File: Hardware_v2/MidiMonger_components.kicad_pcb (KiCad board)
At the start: 2 copper layers, 40 x 100 mm, 58 parts, among them J1 Conn_01x09_Male, J2 Conn_01x08_Male, J3 Conn_01x08_Male, J4 Conn_01x08_Male, J5 SWD_Header, J6 Eurorack_10_pin_power, U1 STM32F446RETx, U2 TL074, U3 74HCT244, U4 MAX5134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

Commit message: Updates to PCB layout
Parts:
- C16: footprint Capacitors_SMD:CP_Elec_5x5.3 -> Capacitor_SMD:CP_Elec_4x5.8
- C17: value 22uF -> 10uF; footprint Capacitors_SMD:CP_Elec_5x5.3 -> Capacitor_SMD:C_0805_2012Metric
- J2: value Conn_01x08_Male -> Conn_01x09_Male; footprint Connector_PinHeader_2.54mm:PinHeader_1x08_P2.54mm_Vertical -> Connector_PinHeader_2.54mm:PinHeader_1x09_P2.54mm_Vertical
- moved C17 68.0 mm to (114.1, 123.0), turned to 180 degrees
- moved R9 56.5 mm to (133.6, 75.9)
- moved R11 54.6 mm to (133.6, 78.4)
- moved R12 48.1 mm to (108.0, 75.7), turned to 0 degrees
- moved R17 44.8 mm to (108.8, 84.6), turned to 0 degrees
- moved R15 44.7 mm to (108.8, 82.9), turned to 0 degrees
- moved R14 44.1 mm to (133.6, 81.1), turned to 180 degrees
- moved R20 43.1 mm to (105.4, 112.5), turned to 0 degrees
- moved J5 38.4 mm to (138.0, 97.9), turned to -90 degrees
- moved R19 38.4 mm to (105.4, 110.9), turned to 0 degrees
- moved U5 37.7 mm to (120.0, 139.0), turned to 0 degrees
- moved R22 35.7 mm to (105.4, 115.7), turned to 0 degrees
- moved R21 33.3 mm to (105.4, 114.1), turned to 0 degrees
- moved R18 31.5 mm to (126.1, 130.5)
- moved R10 29.6 mm to (108.0, 72.3), turned to 0 degrees
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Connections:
- C12 pad 1: VCC -> +12V
- C13 pad 1: VCC -> +12V
- C16 pad 1: VCC -> +12V
- C17 pad 1: GND -> -12V
- C17 pad 2: VEE -> GND
- D2 pad 1: VCC -> +12V
- D2 pad 2: +12V -> /+12V_IN
- D3 pad 1: -12V -> /-12V_IN
- D3 pad 2: VEE -> -12V
- J1 pad 1: /CV1_OUT -> /GATE1_OUT
- J1 pad 2: /CV2_OUT -> /GATE2_LED_OUT
- J1 pad 3: GND -> /GATE3_OUT
- J1 pad 4: /CV3_OUT -> /GATE4_LED_OUT
- J1 pad 5: /CV4_OUT -> GND
- J1 pad 6: /CV1_LED_OUT -> /GATE5_OUT
- J1 pad 7: /CV2_LED_OUT -> /GATE6_LED_OUT
- J1 pad 8: /CV3_LED_OUT -> /GATE7_OUT
- J1 pad 9: /CV4_LED_OUT -> /GATE8_LED_OUT
- J2 pad 2: /GATE1_OUT -> /GATE2_OUT
- J2 pad 3: /GATE2_LED_OUT -> /GATE3_LED_OUT
- J2 pad 4: /GATE2_OUT -> /GATE4_OUT
- J2 pad 5: /GATE3_OUT -> GND
- J2 pad 6: /GATE3_LED_OUT -> /GATE5_LED_OUT
- J2 pad 7: /GATE4_OUT -> /GATE6_OUT
- J2 pad 8: /GATE4_LED_OUT -> /GATE8_OUT
- J3 pad 2: /GATE5_LED_OUT -> /CV1_LED_OUT
- J3 pad 3: GND -> /CV2_LED_OUT
- J3 pad 4: /GATE5_OUT -> /CV3_LED_OUT
- J3 pad 5: /GATE7_OUT -> /CV4_LED_OUT
- J3 pad 6: /USB_DP -> /MIDI_VREF
- J3 pad 7: /USB_DM -> /MIDI_DATA
- J3 pad 8: /USB_VBUS -> unconnected-(J3-Pin_8-Pad8)
- J4 pad 1: /GATE7_LED_OUT -> /USB_VBUS
- J4 pad 2: /GATE6_LED_OUT -> /USB_DM
- J4 pad 3: /GATE8_LED_OUT -> /USB_DP
- J4 pad 4: /GATE6_OUT -> GND
- J4 pad 5: /GATE8_OUT -> /CV3_OUT
- J4 pad 6: GND -> /CV2_OUT
- J4 pad 7: /MIDI_DATA -> /CV1_OUT
- J4 pad 8: /MIDI_VREF -> /CV4_OUT
- J6 pad 1: -12V -> /-12V_IN
- J6 pad 10: +12V -> /+12V_IN
- J6 pad 2: -12V -> /-12V_IN
- J6 pad 9: +12V -> /+12V_IN
- U1 pad 17: /GATE2 -> /GATE8
- U1 pad 21: /GATE3 -> /GATE6
- U1 pad 23: /GATE1 -> /GATE4
- U1 pad 24: unconnected-(U1-PC4-Pad24) -> /GATE2
- U1 pad 25: /GATE4 -> unconnected-(U1-PC5-Pad25)
- U1 pad 26: unconnected-(U1-PB0-Pad26) -> /GATE1
- U1 pad 28: /GATE6 -> /GATE3
- U1 pad 33: unconnected-(U1-PB12-Pad33) -> /GATE5
- U1 pad 35: unconnected-(U1-PB14-Pad35) -> /GATE7
- U1 pad 38: /GATE8 -> unconnected-(U1-PC7-Pad38)
- U1 pad 40: /GATE7 -> unconnected-(U1-PC9-Pad40)
- U1 pad 9: /GATE5 -> unconnected-(U1-PC1-Pad9)
- U2 pad 11: VEE -> -12V
- U2 pad 4: VCC -> +12V
- U6 pad 3: VCC -> +12V
- U7 pad 3: VCC -> +12V
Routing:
- net /CV4_OUT: track 2.87 -> 61.3 mm
- net /NRST: track 0.00 -> 48.4 mm
- net /USB_DP: track 0.00 -> 43.1 mm
- net /USB_DM: track 0.00 -> 41.7 mm
- net /USB_VBUS: track 0.00 -> 40.7 mm
- net /CV1_OUT: track 2.95 -> 35.5 mm
- net /CV3_OUT: track 2.87 -> 33.4 mm
- net /GATE5: track 0.00 -> 28.0 mm
- net /GATE1: track 0.00 -> 26.8 mm
- net /GATE2: track 0.00 -> 26.6 mm
- net /GATE7: track 0.00 -> 26.1 mm
- net /CV4_LED_OUT: track 0.00 -> 25.5 mm
- net /GATE3: track 0.00 -> 24.9 mm
- net /CV3_LED_OUT: track 0.00 -> 24.9 mm
- net /MIDI_DATA: track 0.00 -> 24.6 mm
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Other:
- board text removed: "16"
- board text removed: "3.3VA"
- board text removed: "33"
- board text removed: "49"
- board text removed: "CV LED1-4"
- board text removed: "CV1"
- board text removed: "CV2"
- board text removed: "CV3"
- board text removed: "CV4"
- board text removed: "G1L G1 G2L G2"
- board text removed: "G3 G3L G4 G4L"
- board text removed: "G5"
- board text removed: "G5L"
- board text removed: "G6"
- board text removed: "G7"
- board text removed: "G8"
- board text removed: "GND"
- board text removed: "MD"
- board text removed: "MV"
- board text removed: "RST"
- board text removed: "UDM"
- board text removed: "UDP"
- board text removed: "UVB"

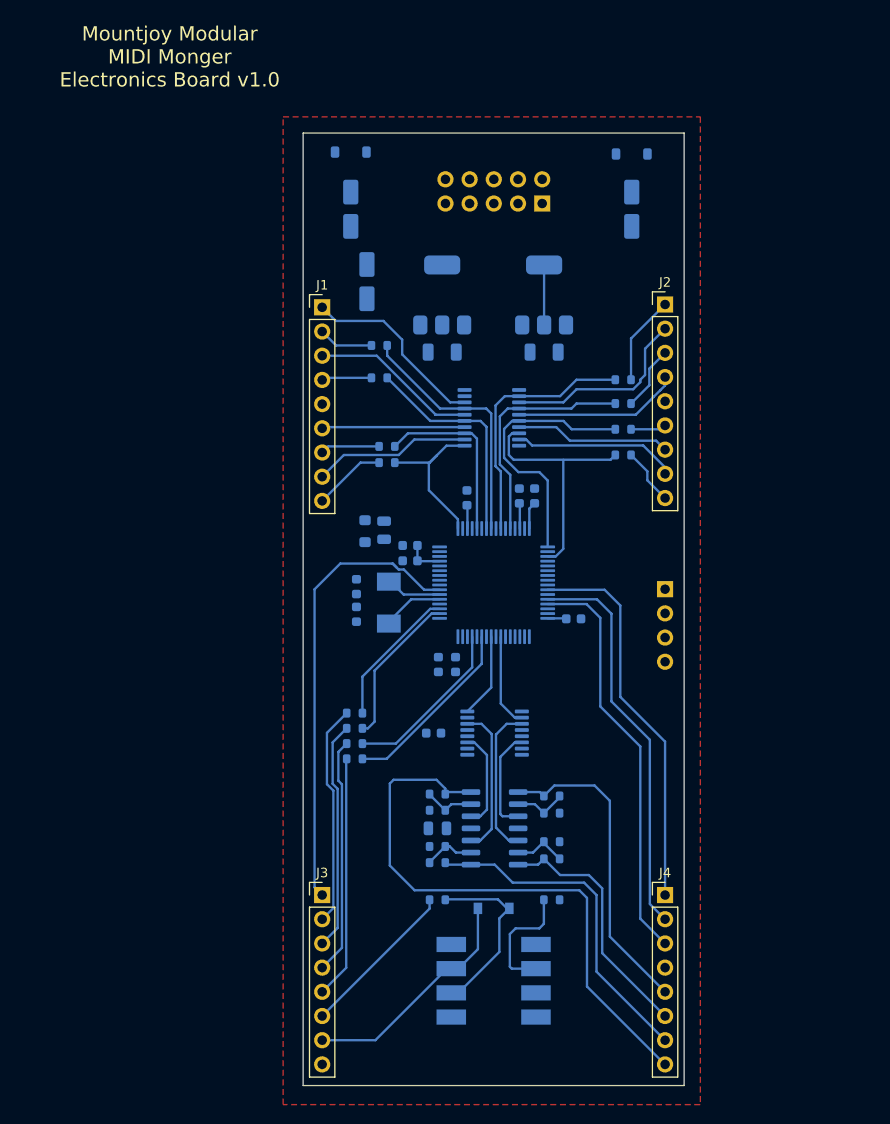
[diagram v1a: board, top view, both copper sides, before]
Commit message: Component PCB first pass routing
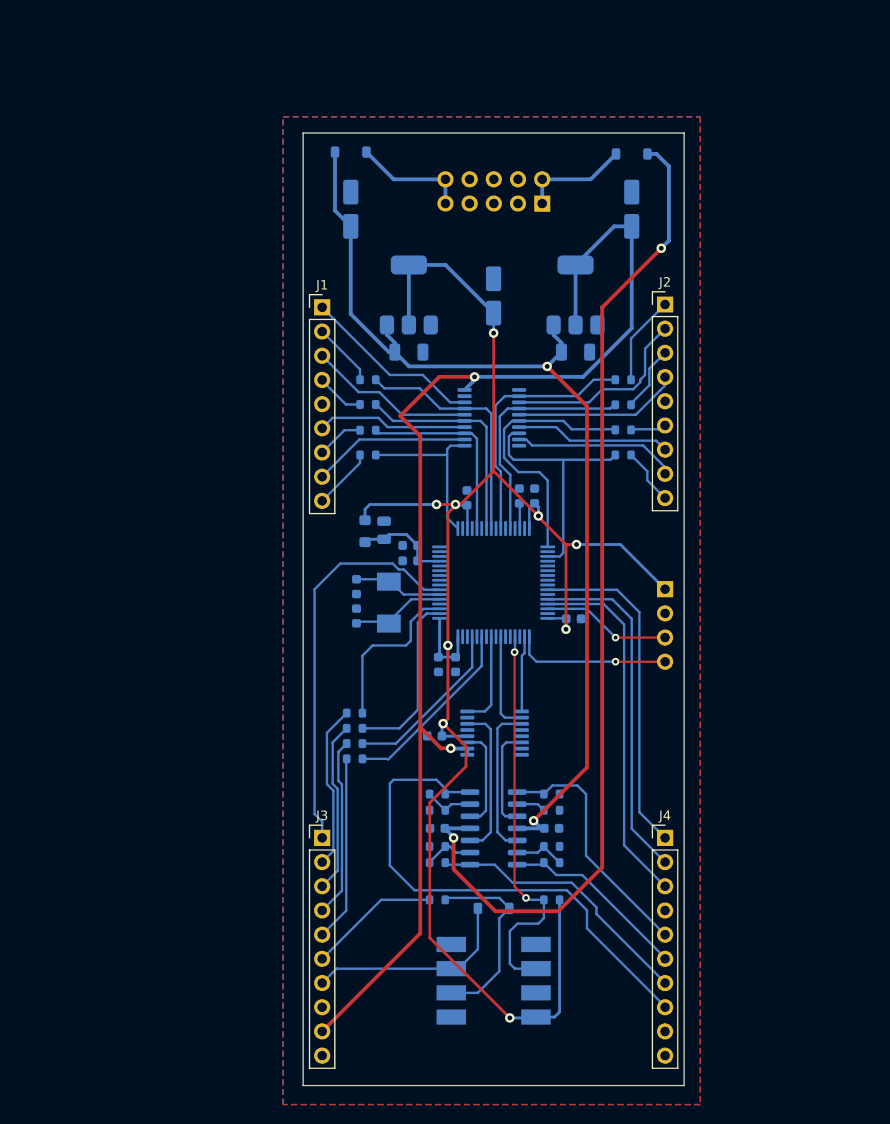
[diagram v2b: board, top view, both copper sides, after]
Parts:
- added C19: 1uF, Capacitor_SMD:C_0603_1608Metric, B.Cu at (126.1, 123.0)
- C17: value 10uF -> 1uF; footprint Capacitor_SMD:C_0805_2012Metric -> Capacitor_SMD:C_0603_1608Metric
- D1: footprint Diodes_SMD:D_SOD-123 -> Diode_SMD:D_SOD-123
- J3, J4: footprint Connector_PinHeader_2.54mm:PinHeader_1x08_P2.54mm_Vertical -> Connector_PinHeader_2.54mm:PinHeader_1x10_P2.54mm_Vertical
- U5: footprint Housings_DIP:DIP-8_W8.89mm_SMDSocket_LongPads -> Package_DIP:DIP-8_W8.89mm_SMDSocket_LongPads
- moved C15 13.4 mm to (120.0, 67.1)
- moved J3 6.00 mm to (102.0, 124.0)
- moved J4 6.00 mm to (138.0, 124.0)
- moved R10 3.79 mm to (106.8, 75.9)
- moved C12 3.50 mm to (111.1, 73.0)
- moved U6 3.50 mm to (111.1, 67.0)
- moved C13 3.30 mm to (128.6, 73.0)
- moved U7 3.30 mm to (128.6, 67.0)
- moved R12 3.05 mm to (106.8, 78.5)
- moved R15 2.62 mm to (106.8, 81.2)
- moved R17 2.15 mm to (106.8, 83.8)
- moved R2 0.50 mm to (126.1, 124.9)
- moved R6 0.40 mm to (126.1, 126.6)
- moved C11 0.32 mm to (113.8, 113.3)
- moved R3 0.30 mm to (126.1, 121.1)
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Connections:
- J3 pad 8: unconnected-(J3-Pin_8-Pad8) -> GND
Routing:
- net +3V3: track 7.25 -> 184.5 mm, vias 0 -> 9
- net +5V: track 6.30 -> 130.9 mm, vias 0 -> 2
- net -12V: track 0.00 -> 105.9 mm, vias 0 -> 2
- net +12V: track 0.00 -> 105.1 mm, vias 0 -> 2
- net /MIDI_RX: track 12.8 -> 42.3 mm, vias 0 -> 2
- net /SWCLK: track 0.00 -> 16.4 mm, vias 0 -> 1
- net /SWDIO: track 0.00 -> 13.6 mm, vias 0 -> 1
- net /+12V_IN: track 0.00 -> 12.0 mm
- net /-12V_IN: track 0.00 -> 11.4 mm
- net /DAC_NSS: track 0.00 -> 7.97 mm
- net /CV3_OUT: track 33.4 -> 26.2 mm
- net /CV4_OUT: track 61.3 -> 54.6 mm
- net /CV1_OUT: track 35.5 -> 28.7 mm
- net /CV2_OUT: track 26.5 -> 19.8 mm
- net /NRST: track 48.4 -> 41.8 mm
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- added copper zone on B.Cu, net GND
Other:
- board text added: "Mountjoy Modular MidiMonger v2.0"
- board text removed: "Mountjoy Modular MIDI Monger Electronics Board v1.0"

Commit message: Started Control layout
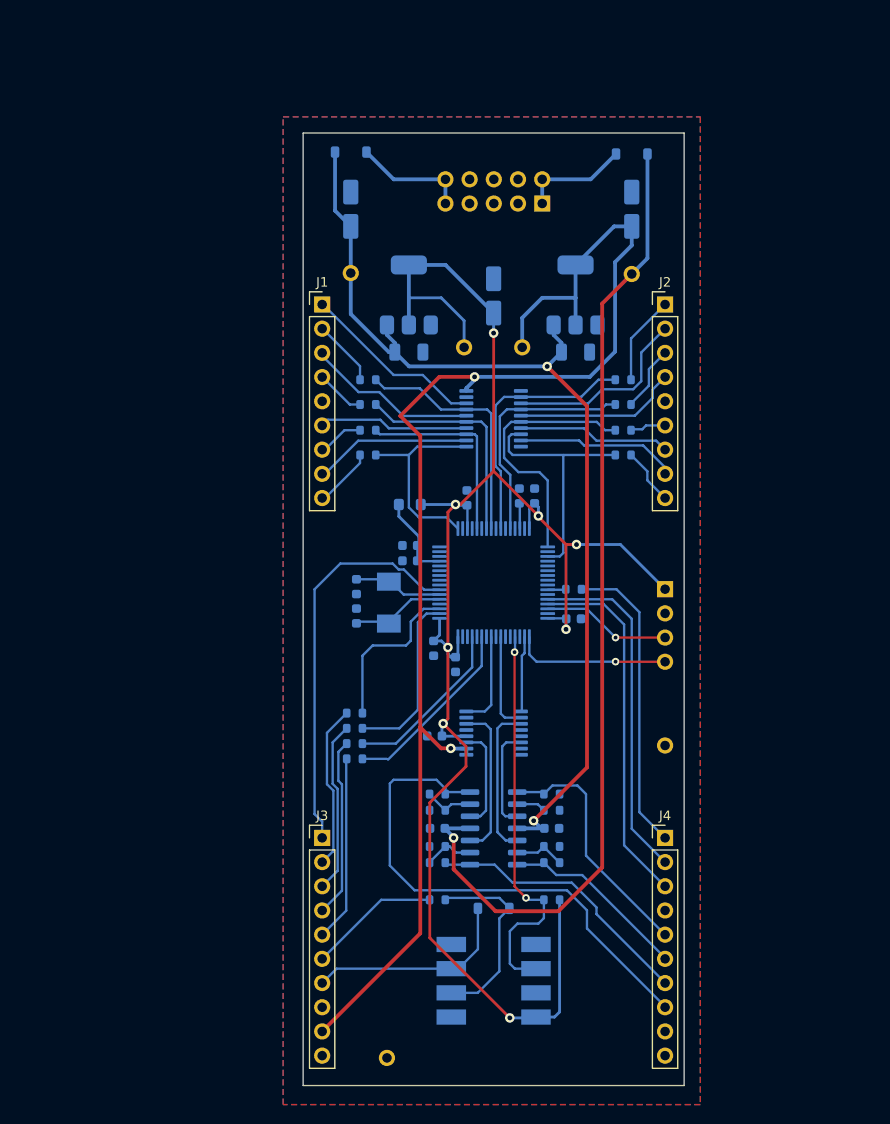
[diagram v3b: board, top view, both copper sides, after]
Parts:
- removed C18: 10uF, Capacitor_SMD:C_0805_2012Metric
- added R23: 10k, Resistor_SMD:R_0603_1608Metric, B.Cu at (128.4, 97.9)
- added TP1: TestPoint, Custom_Footprints:1mm_Test_Point, B.Cu at (105.0, 64.7)
- added TP2: TestPoint, Custom_Footprints:1mm_Test_Point, B.Cu at (134.5, 64.8)
- added TP3: TestPoint, Custom_Footprints:1mm_Test_Point, B.Cu at (116.9, 72.5)
- added TP4: TestPoint, Custom_Footprints:1mm_Test_Point, B.Cu at (123.0, 72.5)
- added TP5: TestPoint, Custom_Footprints:1mm_Test_Point, B.Cu at (138.0, 114.3)
- added TP6: TestPoint, Custom_Footprints:1mm_Test_Point, B.Cu at (108.8, 147.1)
- moved L1 5.47 mm to (111.2, 89.0), turned to 0 degrees
- moved C1 1.77 mm to (113.7, 104.1)
- moved J1 0.30 mm to (102.0, 68.0)
- moved U3 0.21 mm to (120.0, 80.0)
- moved U4 0.10 mm to (120.0, 113.0)
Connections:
- U1 pad 42: /USB_VBUS -> Net-(U1-PA9)
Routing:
- net +5V: track 130.9 -> 140.8 mm
- net /USB_VBUS: track 35.4 -> 31.9 mm
- net /GATE8: track 18.3 -> 21.4 mm
- net -12V: track 105.9 -> 103.5 mm, vias 2 -> 1
- net Net-(U1-PA9): track 0.00 -> 1.92 mm
- net +3V3: track 184.5 -> 185.7 mm, vias 9 -> 8
- net +3.3VA: track 10.3 -> 9.18 mm
- net /GATE3_OUT: track 17.5 -> 18.1 mm
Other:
- board text added: "J1"
- board text added: "J2"
- board text added: "J3"
- board text added: "J4"

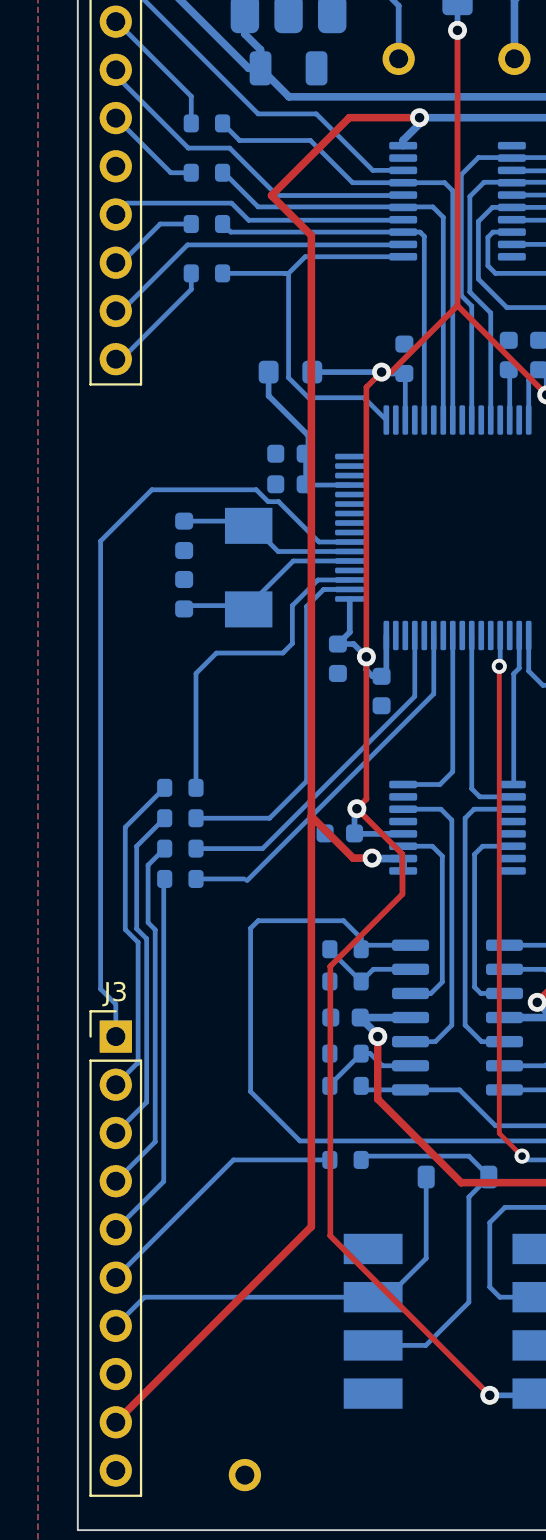
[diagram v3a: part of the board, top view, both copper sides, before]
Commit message: Laying out panel
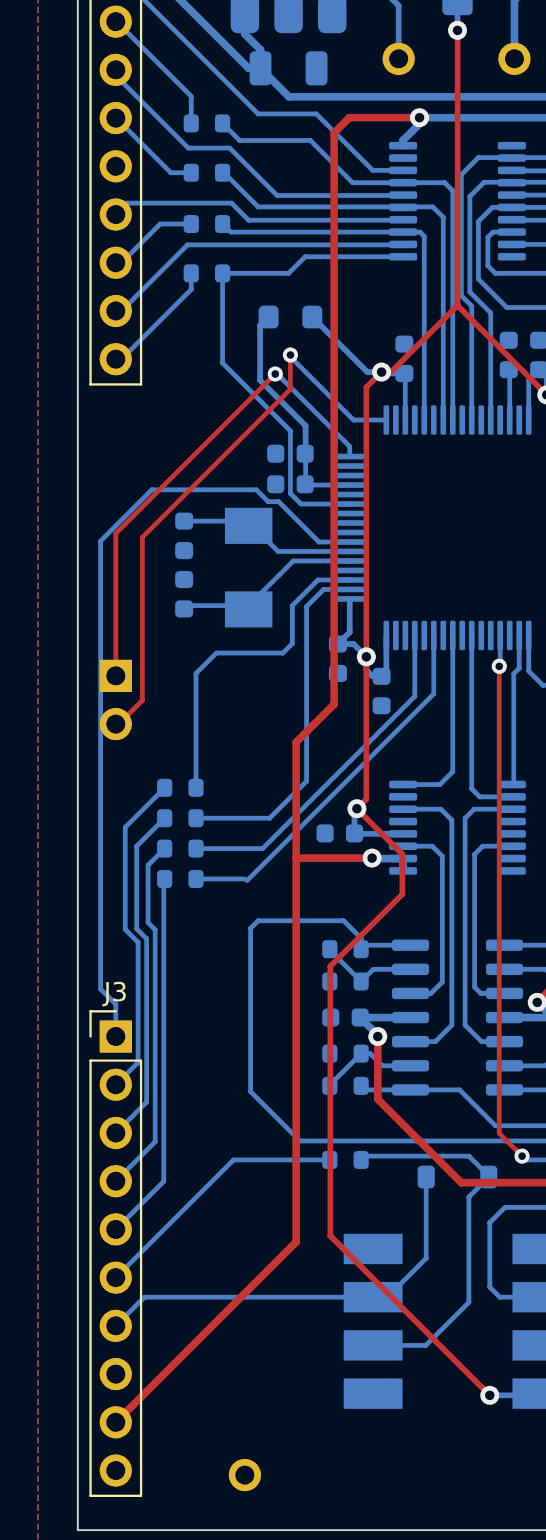
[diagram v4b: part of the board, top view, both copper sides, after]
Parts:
- added J7: UART_Test, Connector_PinHeader_2.54mm:PinHeader_1x02_P2.54mm_Vertical, B.Cu at (102.0, 105.0)
- moved L1 2.90 mm to (111.2, 86.1)
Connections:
- U1 pad 11: unconnected-(U1-PC3-Pad11) -> /GATE8
- U1 pad 16: unconnected-(U1-PA2-Pad16) -> /USART2_TX
- U1 pad 17: /GATE8 -> /USART2_RX
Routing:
- net /USART2_RX: track 0.00 -> 29.9 mm, vias 0 -> 1
- net /USART2_TX: track 0.00 -> 25.4 mm, vias 0 -> 1
- net /GATE8: track 21.4 -> 26.3 mm
- net +3.3VA: track 9.18 -> 12.3 mm
- net +5V: track 140.8 -> 138.9 mm
- net +3V3: track 185.7 -> 186.9 mm
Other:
- board text added: "RX"
- board text added: "TX"

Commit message: Hardware layout
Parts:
- added D4: ESDA6V1BC6, Package_TO_SOT_SMD:SOT-23-6, B.Cu at (131.3, 113.0)
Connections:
- U1 pad 38: unconnected-(U1-PC7-Pad38) -> /MODE_SWITCH
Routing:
- net /MODE_SWITCH: track 0.00 -> 60.1 mm, vias 0 -> 1
- net GND: track 0.00 -> 47.7 mm, vias 0 -> 56
- net /USB_DP: track 38.2 -> 52.6 mm
- net /USB_DM: track 36.7 -> 42.0 mm
- net +5V: track 138.9 -> 143.0 mm
- net /USB_VBUS: track 31.9 -> 34.8 mm
- net +3V3: track 186.9 -> 189.4 mm

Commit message: Gerbers prepared for manufacture
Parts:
- moved TP4 76.2 mm to (111.5, 147.8)
- moved TP3 76.1 mm to (128.1, 147.8)
- moved TP1 35.3 mm to (129.8, 89.8)
- moved TP2 25.0 mm to (134.1, 89.8)
- moved D2 13.9 mm to (107.0, 65.8), turned to -90 degrees
- moved D3 13.7 mm to (132.9, 65.8), turned to -90 degrees
- moved J6 12.3 mm to (125.1, 69.7)
- moved C12 11.9 mm to (111.1, 61.1)
- moved C13 11.9 mm to (128.6, 61.1)
- moved U6 11.9 mm to (111.1, 55.1)
- moved U7 11.9 mm to (128.6, 55.1)
- moved C15 11.9 mm to (120.0, 55.2)
- moved TP6 11.2 mm to (120.0, 147.8)
- moved C14 3.28 mm to (136.2, 55.2)
- moved C16 3.18 mm to (103.5, 55.2)
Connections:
- net /+12V_IN renamed Net-(D2-A)
- net /-12V_IN renamed Net-(D3-K)
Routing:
- net +3V3: track 189.4 -> 207.4 mm
- net -12V: track 103.5 -> 89.7 mm, vias 1 -> 2
- net +12V: track 105.1 -> 117.2 mm
- net +5V: track 143.0 -> 147.0 mm
- net GND: track 47.7 -> 45.7 mm, vias 56 -> 66
- net Net-(D2-A): track 12.0 -> 10.6 mm
